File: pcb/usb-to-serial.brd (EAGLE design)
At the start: 50 x 20 mm, 34 parts, among them CON1 MLW10G, IC1 FT231XS, IC2 STMPS2141STR, IC3 CAT6219-330TDGT3, J1 MINI B, J2 MICRO B, J3 EXT

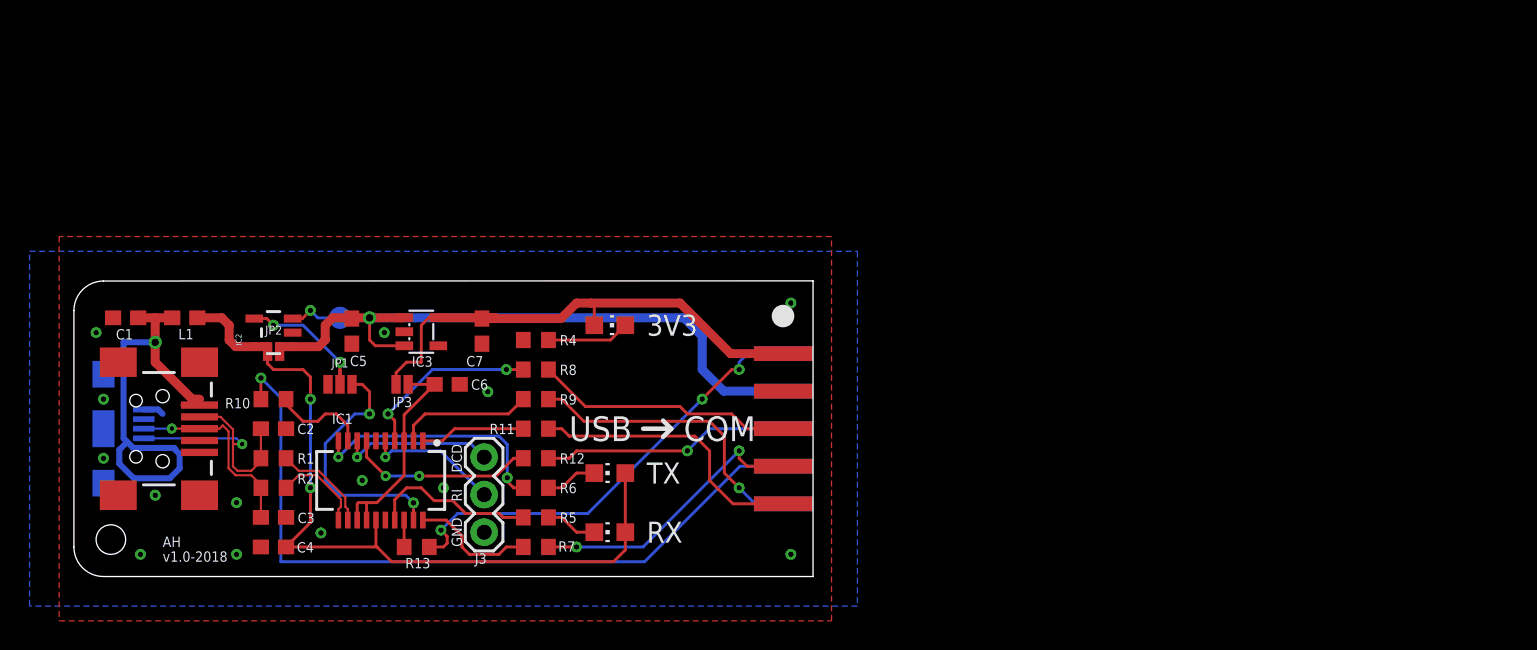
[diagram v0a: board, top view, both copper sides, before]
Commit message: Update to v2
Changes from Issues:
- Pinout on top/bottom silkscreen
- Add indication LED to error output of IC2 (over current shutdown)
- Add EN pin of IC2 to EXT connector
- Add OSHW logo to silkscreen
Replace mini USB connector with USB-C
- Replace IC3 with XC6210
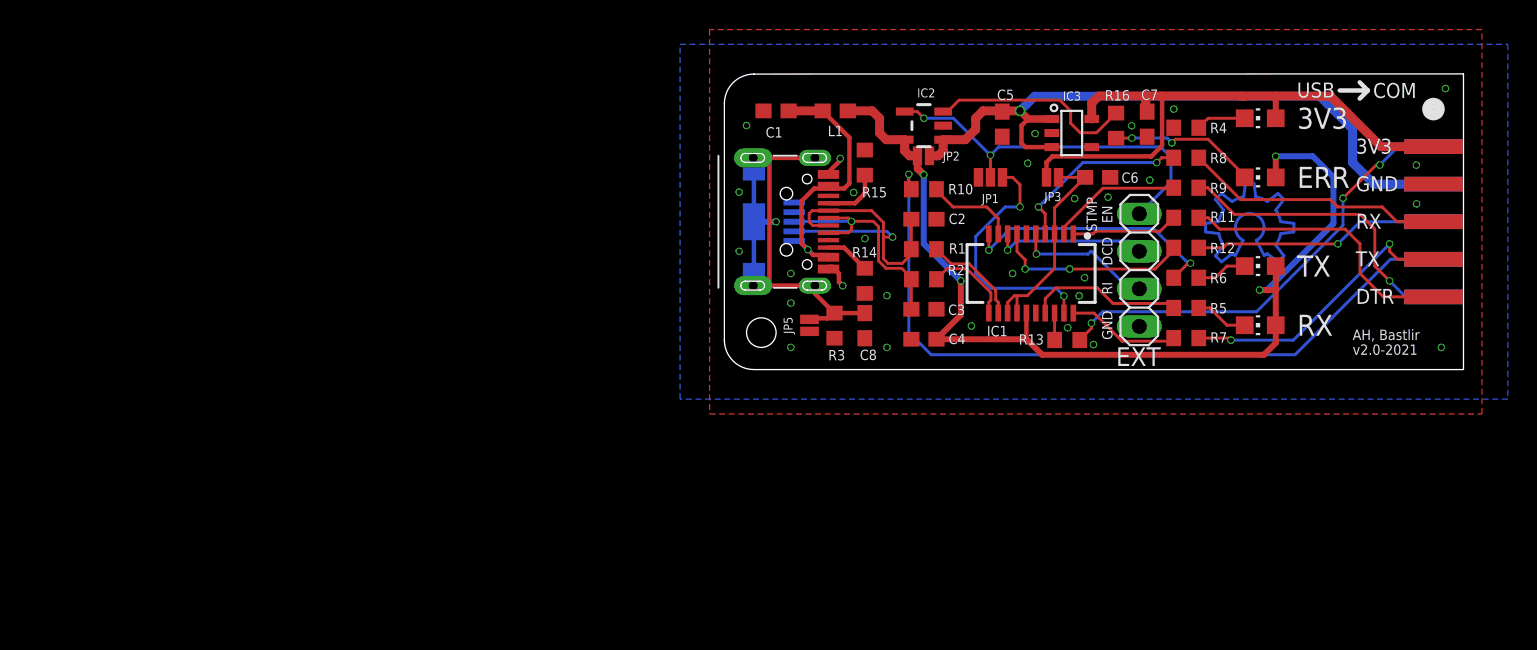
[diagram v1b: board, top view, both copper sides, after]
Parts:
- removed J3: EXT, SparkFun-Connectors:1X03
- removed TP1: TEST_POINT-1.5, testpoints:TP_1.5MM
- added C8: 100nF, rcl:C0603
- added D1: (no value), led:CHIP-LED0805
- added EXT: J3, pinhead:1X04
- added JP5: JUMPER-SMT_2_NO_NO-SILK, SparkFun-Jumpers:SMT-JUMPER_2_NO_NO-SILK
- added R14, R15: 5k1, rcl:R0603
- added R16: 270, rcl:R0603
- added R3: 0, rcl:R0603
- IC3: value CAT6219-330TDGT3 -> XC6210; device ic-power:TSOT23-5L -> Bastlir:SOT-23-5
- J1: value MINI B -> HRO_31_M_12_USB_C; device SparkFun-Connectors:USB-MINIB -> Bastlir:HRO_31_M_12_USB_C
- moved C7 47.1 mm to (72.6, 30.6)
- moved R4 46.3 mm to (75.2, 30.4)
- moved R8 46.3 mm to (75.2, 28.3)
- moved R9 46.3 mm to (75.2, 26.3)
- moved R11 46.2 mm to (75.2, 24.3)
- moved R12 46.2 mm to (75.2, 22.2)
- moved R10 46.2 mm to (57.5, 26.2)
- moved R6 46.2 mm to (75.2, 20.2)
- moved C2 46.2 mm to (57.5, 24.2)
- moved R1 46.2 mm to (57.5, 22.1)
- moved R5 46.2 mm to (75.2, 18.2)
- moved R2 46.2 mm to (57.5, 20.1)
- moved R7 46.2 mm to (75.2, 16.1)
- moved C3 46.2 mm to (57.5, 18.1)
- moved C4 46.2 mm to (57.5, 16.1)
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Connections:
- removed net N$4: C1.1, J1.VBUS, J2.VBUS, L1.2
- removed net N$6: IC2.3, TP1.TP
- new net N$11: D1.C, R16.2
- new net N$7: J1.B5, R14.2
- new net N$8: C8.1, J1.S1, J1.S2, J1.S3, J1.S4, J2.SHIELD1, J2.SHIELD2, J2.SHIELD3, JP5.2, R3.2
- new net STMP_EN: EXT.4, IC2.4, JP1.2
- new net STMP_ERR: IC2.3, R16.1
- new net VBUS: C1.1, J1.A4, J1.A9, J1.B4, J1.B9, J2.VBUS, L1.2
- net +5V: now also D1.A
- net DCD: now also EXT.3; no longer J3.3
- net GND: now also C8.2, EXT.1, J1.A1, J1.A12, J1.B1, J1.B12, JP5.1, R14.1, R15.1, R3.1; no longer J1.GND, J1.S1, J1.S2, J1.S3, J1.S4, J2.SHIELD1, J2.SHIELD2, J2.SHIELD3, J3.1
- net N$2: now also J1.A5, R15.2; no longer IC2.4, JP1.2
- net RI: now also EXT.2; no longer J3.2
- net USBD_N: now also J1.A7, J1.B7; no longer J1.D-
- net USBD_P: now also J1.A6, J1.B6; no longer J1.D+
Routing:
- net N$8: track 0.00 -> 32.6 mm, vias 0 -> 1
- net STMP_EN: track 0.00 -> 26.0 mm, vias 0 -> 2
- net VBUS: track 0.00 -> 18.5 mm, vias 0 -> 1
- net +5V: track 54.0 -> 69.0 mm, vias 2 -> 4
- net STMP_ERR: track 0.00 -> 14.0 mm
- net N$11: track 0.00 -> 10.1 mm, vias 0 -> 2
- net 3V3_OUT: track 35.3 -> 41.4 mm
- net N$2: track 9.52 -> 3.98 mm, vias 2 -> 0
- net USBD_N: track 17.0 -> 22.0 mm
- net N$4: track 31.2 -> 27.2 mm, vias 1 -> 0
- net N$6: track 3.63 -> 0.00 mm, vias 1 -> 0
- net USBD_P: track 13.3 -> 16.8 mm
- net N$7: track 0.00 -> 3.03 mm
- net GND: track 1.40 -> 3.69 mm, vias 14 -> 29
- net N$5: track 5.61 -> 3.38 mm
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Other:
- board text added: "3V3 GND RX TX DTR"
- board text added: "AH, Bastlir"
- board text added: "ERR"
- board text added: "STMP EN"
- board text added: "TXDEN 5V_OUT DSR CTS RTS"
- board text added: "v2.0-2021"
- board text removed: "AH"
- board text removed: "v1.0-2018"

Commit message: Polishing of v2 according to notes from Adam, added schematic in PDF, gerber ZIP package.
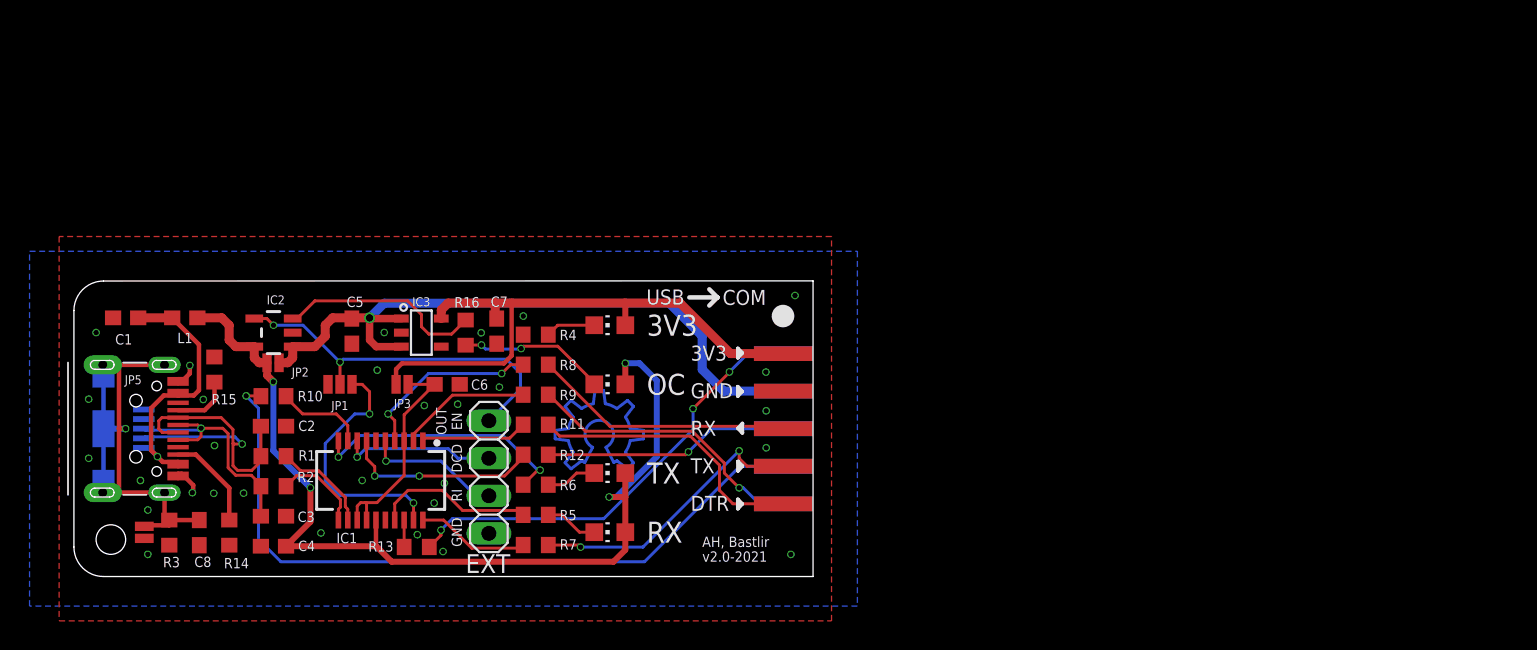
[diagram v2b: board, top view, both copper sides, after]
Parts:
- C7: value 2.2uF -> 1uF
- IC3: value XC6210 -> XC6210B332MR
- moved C8 47.1 mm to (8.48, 2.97)
- moved JP5 47.1 mm to (4.76, 2.99)
- moved R3 47.1 mm to (6.45, 2.97)
- moved R14 46.2 mm to (10.5, 2.97)
- moved C1 46.2 mm to (3.50, 17.5)
- moved C2 46.2 mm to (13.5, 10.2)
- moved C3 46.2 mm to (13.5, 4.08)
- moved C4 46.2 mm to (13.5, 2.05)
- moved C5 46.2 mm to (18.8, 16.6)
- moved C6 46.2 mm to (25.2, 13.0)
- moved CON1 46.2 mm to (50.0, 10.0)
- moved D1 46.2 mm to (36.2, 13.0)
- moved D2 46.2 mm to (36.2, 17.0)
- moved D3 46.2 mm to (36.2, 3.00)
- moved D4 46.2 mm to (36.2, 7.00)
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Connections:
- net STMP_EN renamed OUT_EN
- net STMP_ERR renamed OC_ERR
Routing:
- net N$7: track 3.03 -> 6.57 mm
- net +5V: track 69.0 -> 66.7 mm
- net RTS: track 20.4 -> 19.4 mm
- net CTS: track 50.6 -> 49.9 mm
- net 3V3_OUT: track 41.4 -> 40.7 mm
- net OUT_EN: track 26.0 -> 25.3 mm
- net GND: track 3.69 -> 3.98 mm, vias 29 -> 30
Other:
- board text added: "OC"
- board text added: "OUT EN"
- board text removed: "ERR"
- board text removed: "STMP EN"
